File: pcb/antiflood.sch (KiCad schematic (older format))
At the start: 94 parts, among them J1 Barrel_Jack, J10 Screw_Terminal_01x02, J11 Screw_Terminal_01x02, J12 Screw_Terminal_01x02, J13 Screw_Terminal_01x02, J2 01x03, J3 01x03, J5 Conn_02x04_Odd_Even, J6 Conn_02x05_Odd_Even, J7 Conn_02x03_Odd_Even, J8 Screw_Terminal_01x02, J9 Screw_Terminal_01x02, K1 P-5, K2 P-5, Q1 2N3904, Q2 2N3904, SW1 SW_Push, SW2 SW_Push, SW3 SW_Push, U1 LM1117-3.3, U2 ATMEGA328P-AU, U4 MC34063, U6 TP4056, Y1 16MHz

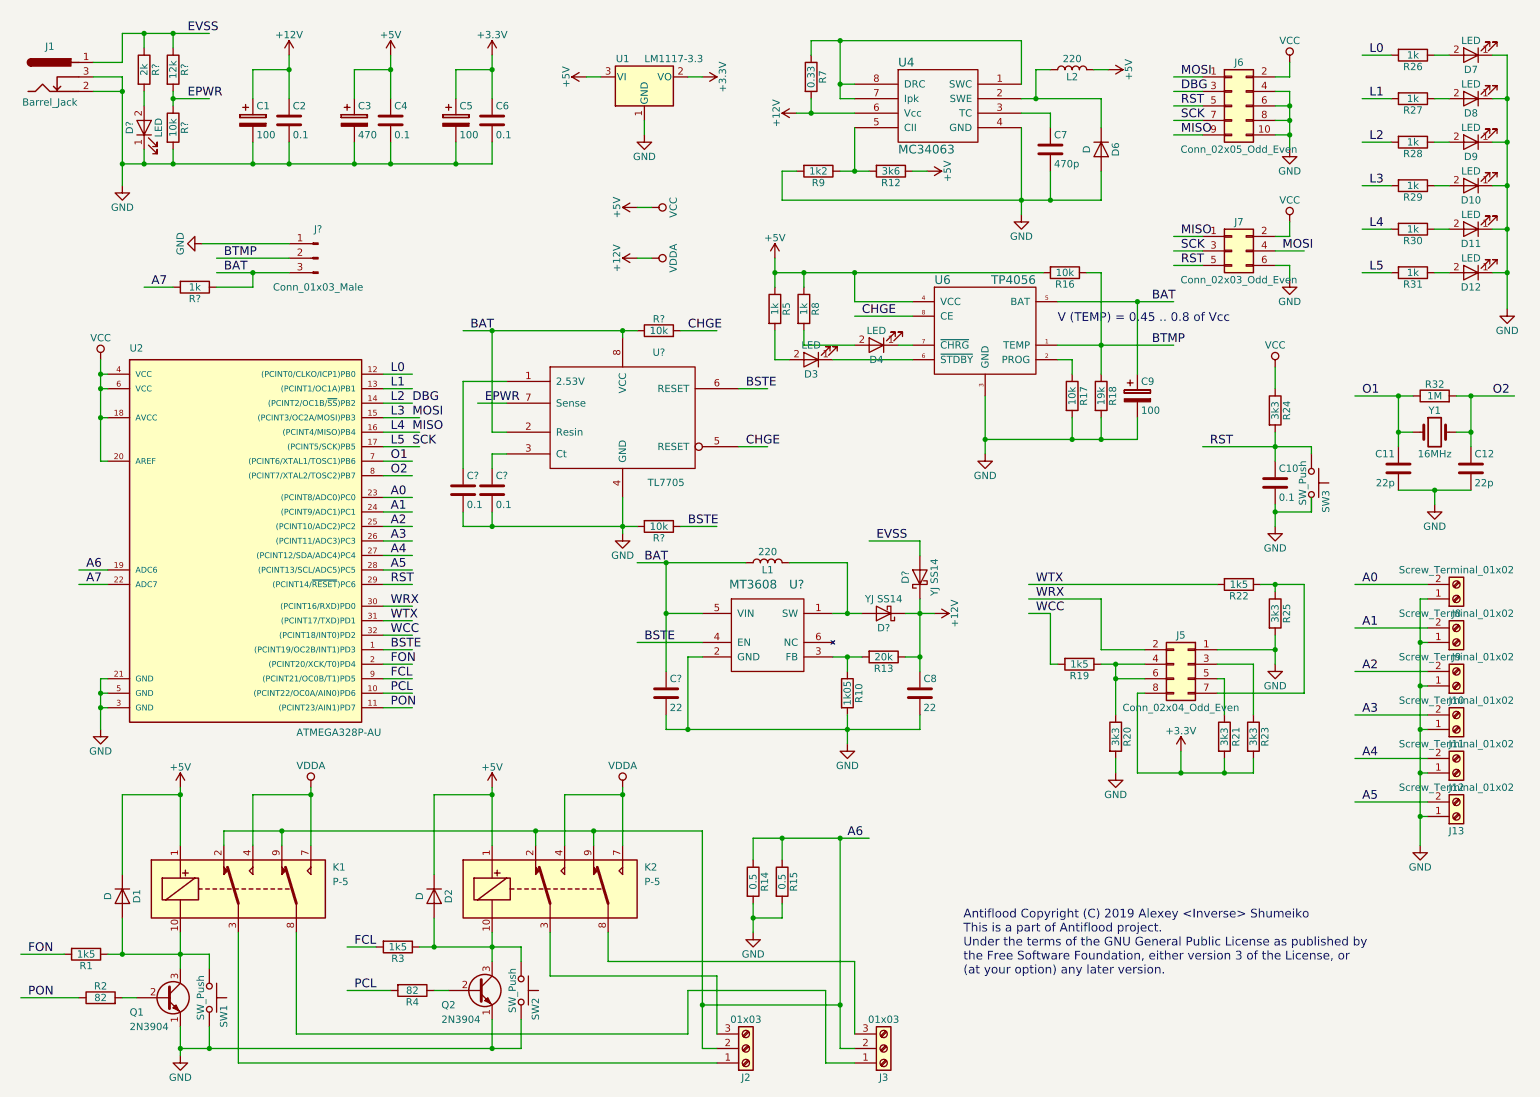
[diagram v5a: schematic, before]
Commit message: PCB: power units placement
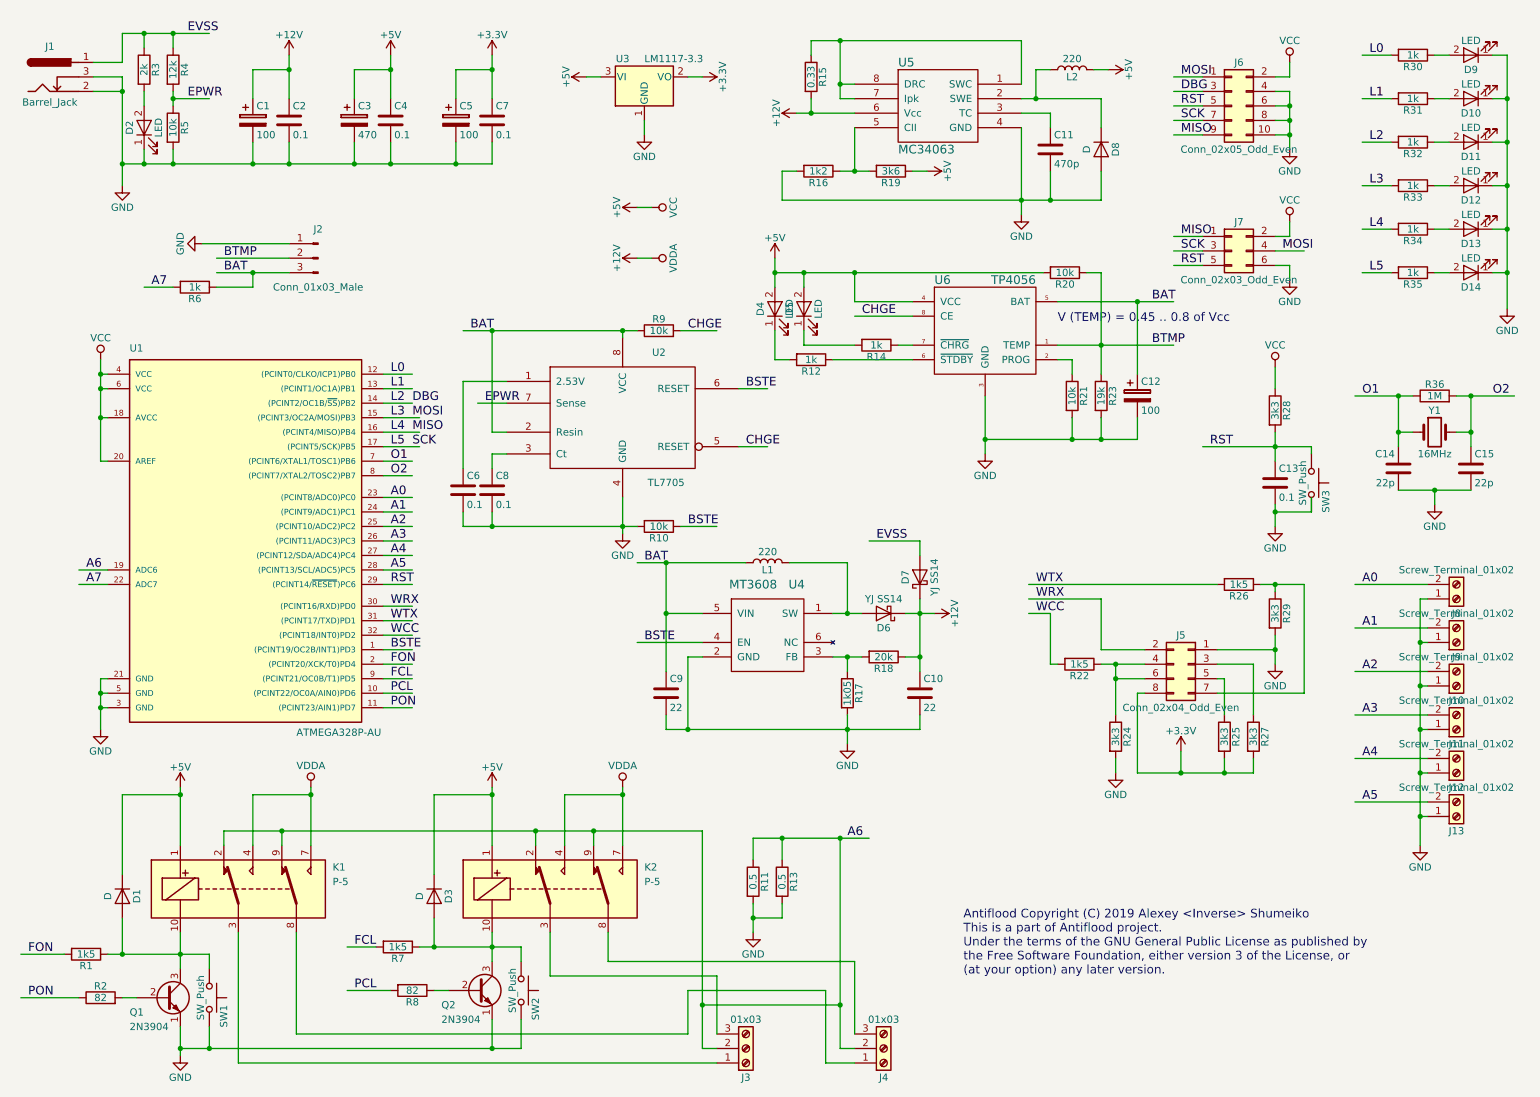
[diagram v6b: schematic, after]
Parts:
- C9: renamed from C?; footprint (none) -> Capacitors_SMD:C_1206
- D2: renamed from D?; footprint (none) -> LEDs:LED_1206
- D6, D7: renamed from D?; footprint (none) -> Diodes_SMD:D_SMA
- J2: renamed from J?; footprint (none) -> Pin_Headers:Pin_Header_Straight_1x03_Pitch2.54mm
- R10, R3, R4, R5, R6, R9: renamed from R?; footprint (none) -> Resistors_SMD:R_0805
- U2: renamed from U?; footprint (none) -> SMD_Packages:SOIC-8-N
- U4: renamed from U?; footprint (none) -> SMD_Packages:Ceramic_Filter
- gave numbers to parts that had none: 2
- renumbered C8 to C10, C7 to C11, C9 to C12, C10 to C13, C11 to C14, C12 to C15, C6 to C7, D8 to D10, D9 to D11, D10 to D12, D11 to D13, D12 to D14, D2 to D3, D3 to D4, D4 to D5, D6 to D8, D7 to D9, J2 to J3, J3 to J4, R14 to R11, R5 to R12, R15 to R13, R8 to R14, R7 to R15, R9 to R16, R10 to R17, R13 to R18, R12 to R19, R16 to R20, R17 to R21, R19 to R22, R18 to R23, R20 to R24, R21 to R25, R22 to R26, R23 to R27, R24 to R28, R25 to R29, R26 to R30, R27 to R31, R28 to R32, R29 to R33, R30 to R34, R31 to R35, R32 to R36, R3 to R7, R4 to R8, U2 to U1, U1 to U3, U4 to U5
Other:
- moved on the sheet: D4, D5, R12, R14

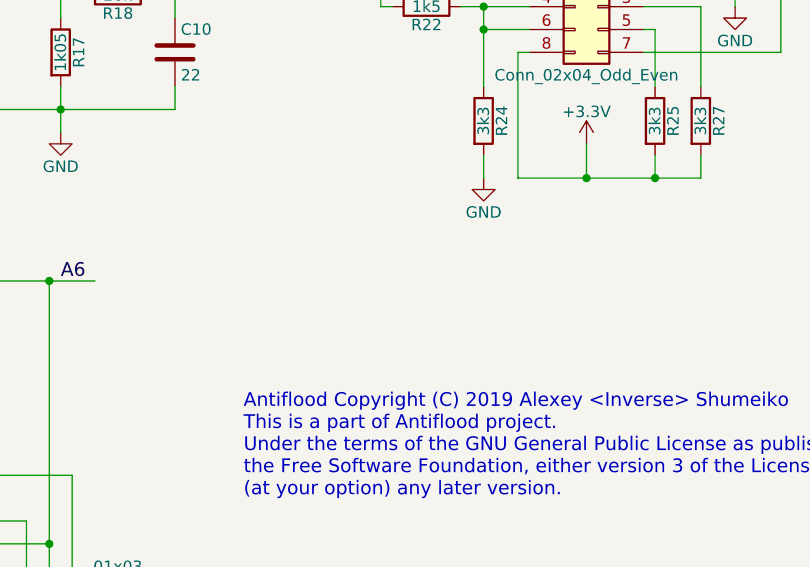
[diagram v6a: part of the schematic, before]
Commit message: PCB: alt placement
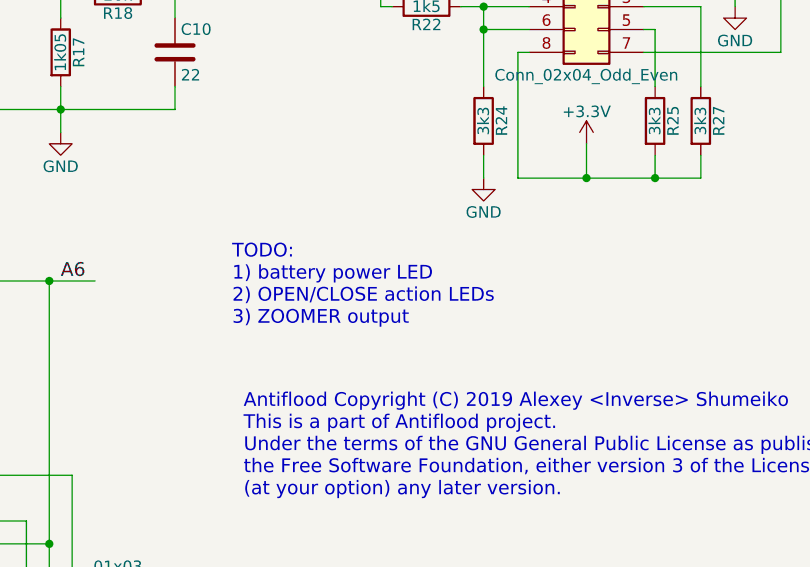
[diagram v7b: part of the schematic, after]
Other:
- note added: "TODO:\n1) battery power LED\n2) OPEN/CLOSE action LEDs\n3) ZOOMER output"
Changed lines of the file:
@@
 Wire Wire Line
 	6750 4050 6400 4050
+Text Notes 7000 6300 0    60   ~ 0
+TODO:\n1) battery power LED\n2) OPEN/CLOSE action LEDs\n3) ZOOMER output
 $EndSCHEMATC

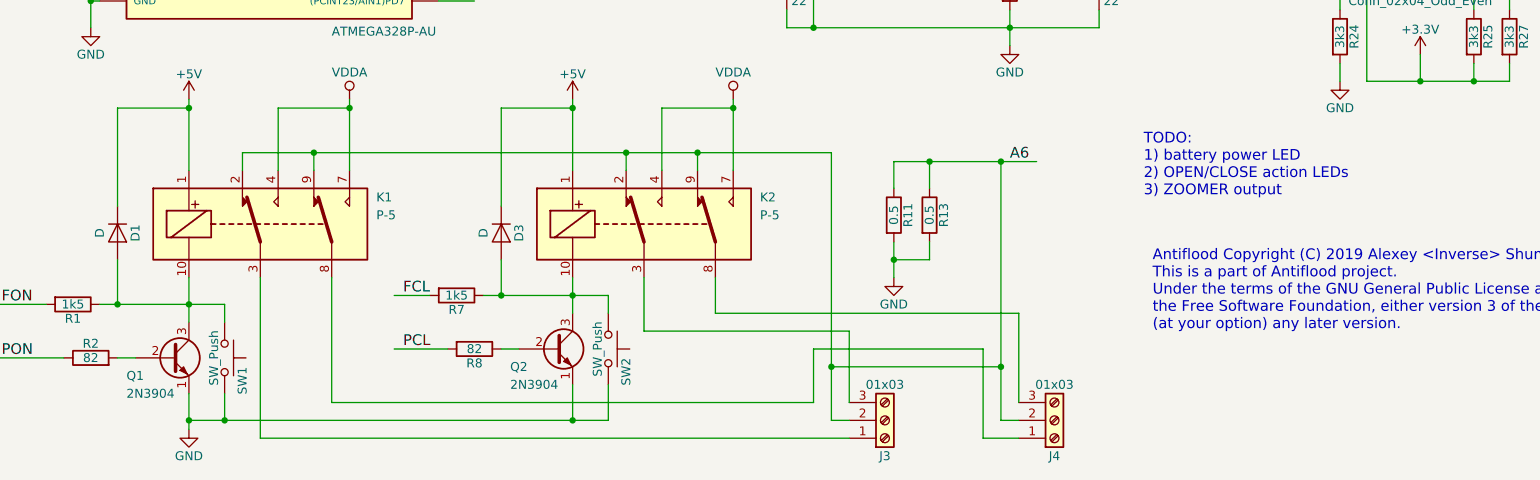
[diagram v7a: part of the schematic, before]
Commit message: PCB: smd transistors, components placement
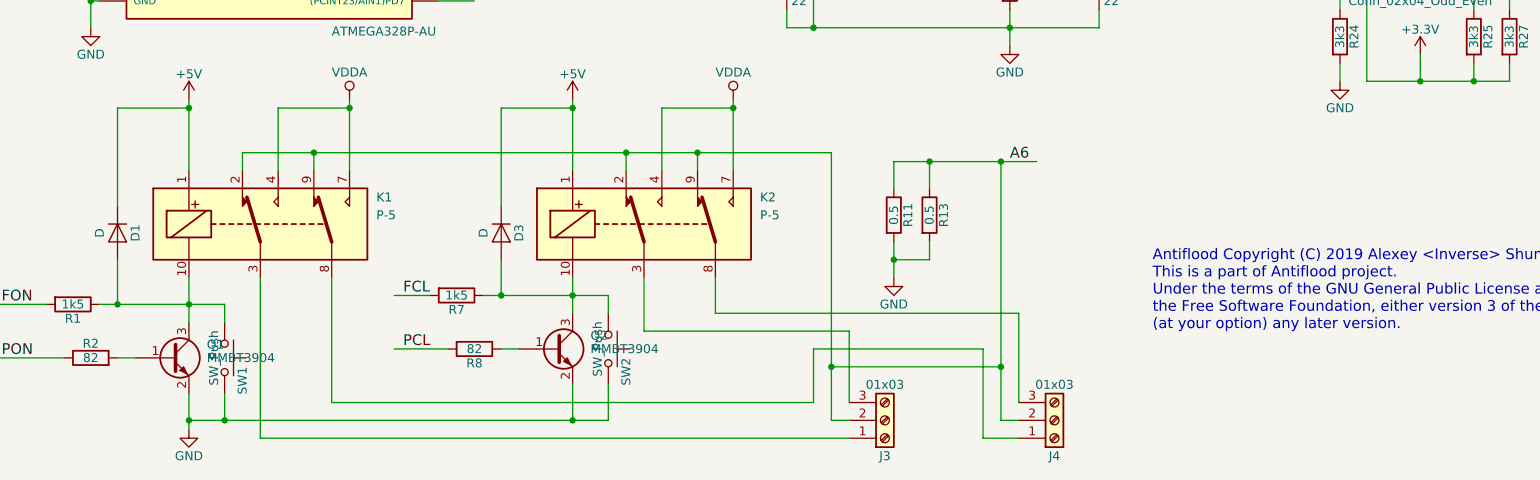
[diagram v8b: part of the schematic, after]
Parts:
- removed Q1, Q2: 2N3904, TO_SOT_Packages_THT:TO-92_Molded_Narrow, symbol 2N3904
- added Q1, Q2: MMBT3904, TO_SOT_Packages_SMD:SOT-23, symbol MMBT3904
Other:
- note removed: "TODO:\n1) battery power LED\n2) OPEN/CLOSE action LEDs\n3) ZOOMER output"
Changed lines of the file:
@@
-$EndComp
-$Comp
-L 2N3904 Q1
-U 1 1 5B459296
-P 1550 7200
-F 0 "Q1" H 1300 7100 50  0000 L CNN
-F 1 "2N3904" H 1300 7000 50  0000 L CNN
-F 2 "TO_SOT_Packages_THT:TO-92_Molded_Narrow" H 1750 7125 50  0001 L CIN
-F 3 "" H 1550 7200 50  0001 L CNN
-	1    1550 7200
-	1    0    0    -1
 $EndComp
 $Comp
@@
 F 3 "" H 2550 5750 50  0001 C CNN
 	1    2550 5750
-	1    0    0    -1
-$EndComp
-$Comp
-L 2N3904 Q2
-U 1 1 5B8B1FB0
-P 3700 7150
-F 0 "Q2" H 3450 7050 50  0000 L CNN
-F 1 "2N3904" H 3450 6950 50  0000 L CNN
-F 2 "TO_SOT_Packages_THT:TO-92_Molded_Narrow" H 3900 7075 50  0001 L CIN
-F 3 "" H 3700 7150 50  0001 L CNN
-	1    3700 7150
 	1    0    0    -1
 $EndComp
@@
 Wire Wire Line
 	6750 4050 6400 4050
-Text Notes 7000 6300 0    60   ~ 0
-TODO:\n1) battery power LED\n2) OPEN/CLOSE action LEDs\n3) ZOOMER output
+$Comp
+L MMBT3904 Q1
+U 1 1 5CC995C3
+P 1550 7200
+F 0 "Q1" H 1750 7275 50  0000 L CNN
+F 1 "MMBT3904" H 1750 7200 50  0000 L CNN
+F 2 "TO_SOT_Packages_SMD:SOT-23" H 1750 7125 50  0001 L CIN
+F 3 "" H 1550 7200 50  0001 L CNN
+	1    1550 7200
+	1    0    0    -1
+$EndComp
+$Comp
+L MMBT3904 Q2
+U 1 1 5CC99713
+P 3700 7150
+F 0 "Q2" H 3900 7225 50  0000 L CNN
+F 1 "MMBT3904" H 3900 7150 50  0000 L CNN
+F 2 "TO_SOT_Packages_SMD:SOT-23" H 3900 7075 50  0001 L CIN
+F 3 "" H 3700 7150 50  0001 L CNN
+	1    3700 7150
+	1    0    0    -1
+$EndComp
 $EndSCHEMATC
